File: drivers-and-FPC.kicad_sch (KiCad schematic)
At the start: 0 parts

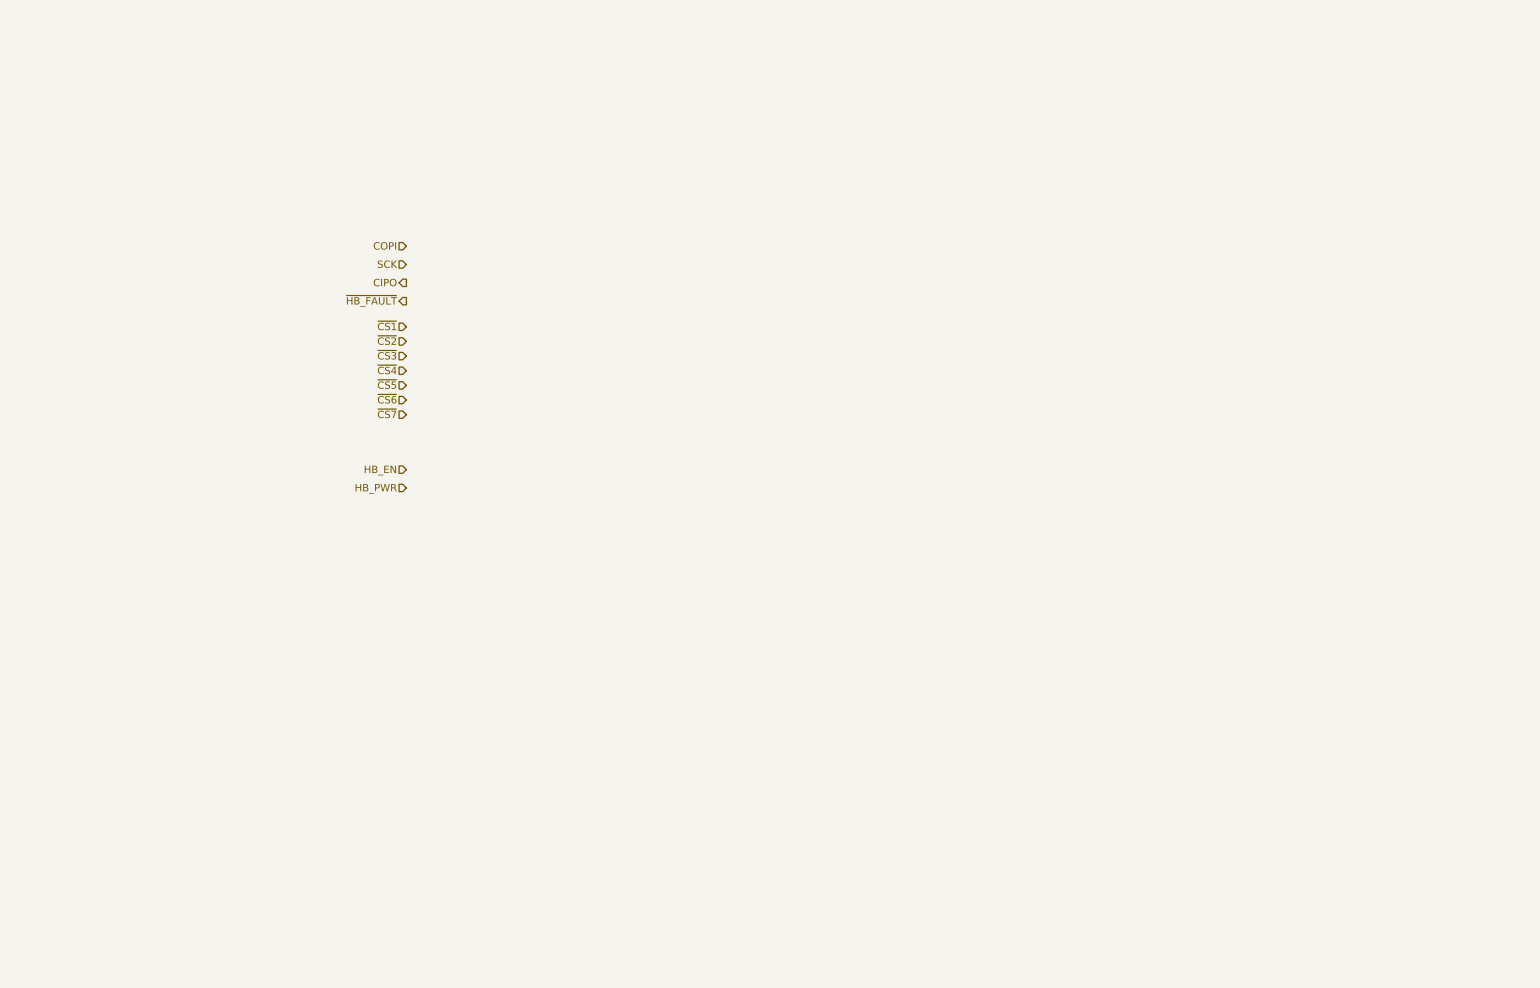
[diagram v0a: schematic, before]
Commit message: schematic rough draft except fpc
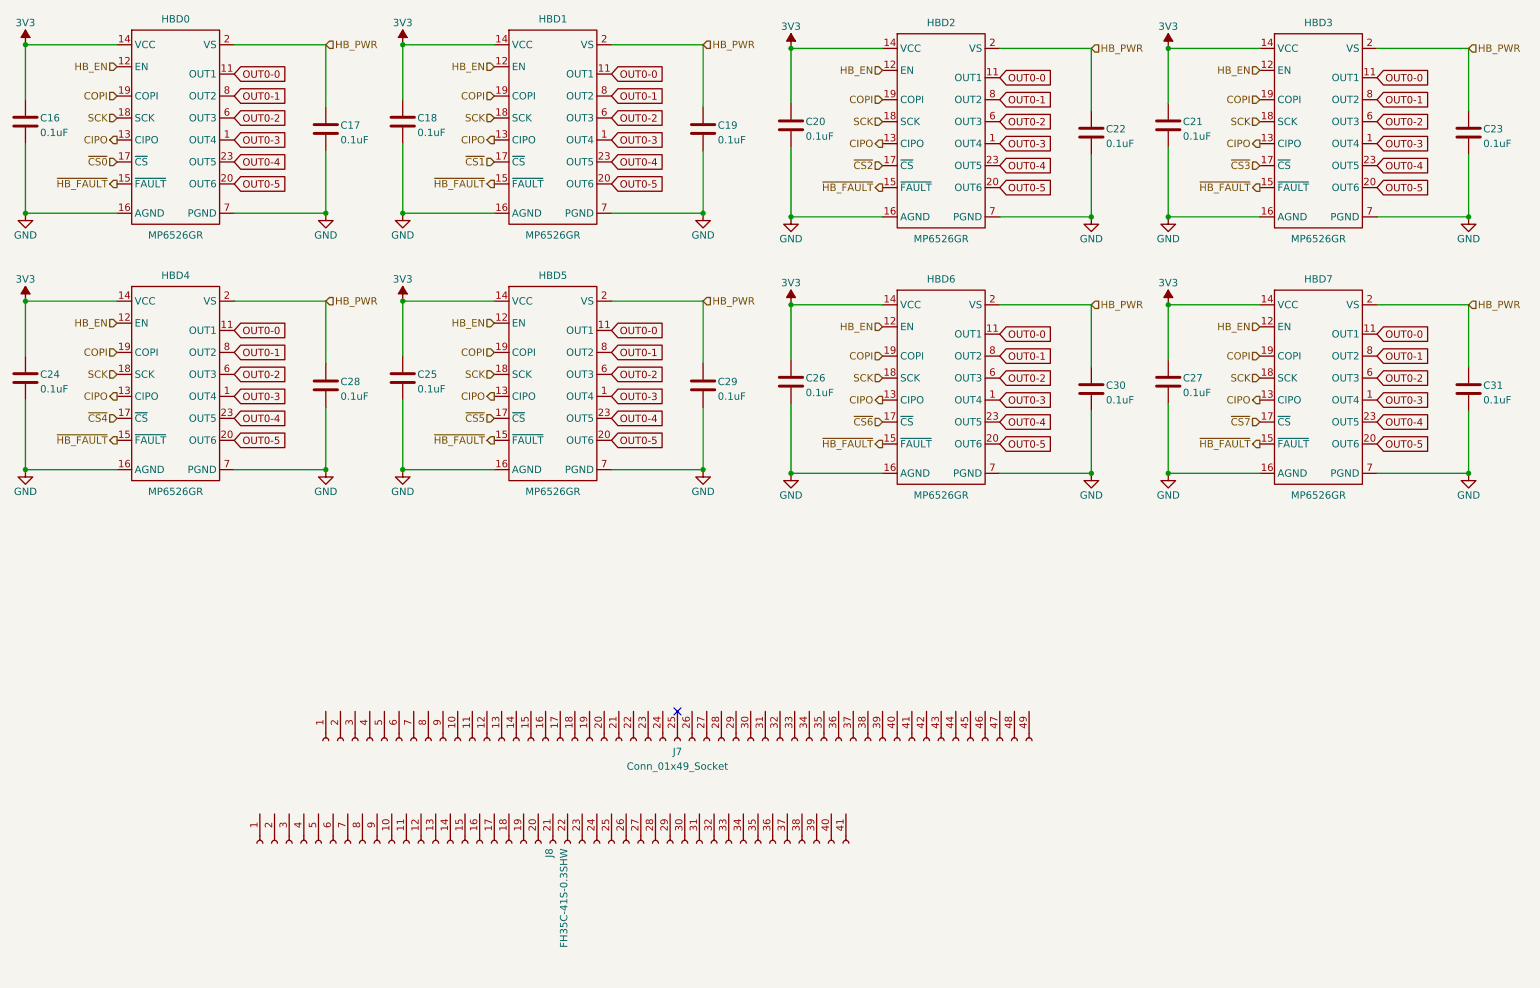
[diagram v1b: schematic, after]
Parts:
- added C16, C17, C18, C19, C20, C21, C22, C23, C24, C25, C26, C27, C28, C29, C30, C31: 0.1uF, Capacitor_SMD:C_0402_1005Metric, symbol Device:C
- added HBD0, HBD1, HBD2, HBD3, HBD4, HBD5, HBD6, HBD7: MP6526GR, Package_DFN_QFN:QFN-24-1EP_4x4mm_P0.5mm_EP2.7x2.7mm, symbol nrf52-controller:MP6526
- added J7: Conn_01x49_Socket, symbol Connector:Conn_01x49_Socket
- added J8: FH35C-41S-0.3SHW, v12e:CONN_FH35W-41S-0.3SHW, symbol v12e:Conn_01x41_Socket
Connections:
- net CIPO: now also HBD0.13 (CIPO), HBD1.13 (CIPO), HBD2.13 (CIPO), HBD3.13 (CIPO), HBD4.13 (CIPO), HBD5.13 (CIPO), HBD6.13 (CIPO), HBD7.13 (CIPO)
- net COPI: now also HBD0.19 (COPI), HBD1.19 (COPI), HBD2.19 (COPI), HBD3.19 (COPI), HBD4.19 (COPI), HBD5.19 (COPI), HBD6.19 (COPI), HBD7.19 (COPI)
- net HB_EN: now also HBD0.12 (EN), HBD1.12 (EN), HBD2.12 (EN), HBD3.12 (EN), HBD4.12 (EN), HBD5.12 (EN), HBD6.12 (EN), HBD7.12 (EN)
- net SCK: now also HBD0.18 (SCK), HBD1.18 (SCK), HBD2.18 (SCK), HBD3.18 (SCK), HBD4.18 (SCK), HBD5.18 (SCK), HBD6.18 (SCK), HBD7.18 (SCK)
- net ~{CS1}: now also HBD1.17 (~{CS})
- net ~{CS2}: now also HBD2.17 (~{CS})
- net ~{CS3}: now also HBD3.17 (~{CS})
- net ~{CS4}: now also HBD4.17 (~{CS})
- net ~{CS5}: now also HBD5.17 (~{CS})
- net ~{CS6}: now also HBD6.17 (~{CS})
- net ~{CS7}: now also HBD7.17 (~{CS})
- net ~{HB_FAULT}: now also HBD0.15 (~{FAULT}), HBD1.15 (~{FAULT}), HBD2.15 (~{FAULT}), HBD3.15 (~{FAULT}), HBD4.15 (~{FAULT}), HBD5.15 (~{FAULT}), HBD6.15 (~{FAULT}), HBD7.15 (~{FAULT})
- new net 3V3: C16.1, C18.1, C20.1, C21.1, C24.1, C25.1, C26.1, C27.1, HBD0.14 (VCC), HBD1.14 (VCC), HBD2.14 (VCC), HBD3.14 (VCC), HBD4.14 (VCC), HBD5.14 (VCC), HBD6.14 (VCC), HBD7.14 (VCC)
- new net GND: C16.2, C17.2, C18.2, C19.2, C20.2, C21.2, C22.2, C23.2, C24.2, C25.2, C26.2, C27.2, C28.2, C29.2, C30.2, C31.2, HBD0.10 (PGND), HBD0.16 (AGND), HBD0.21 (PGND), HBD0.22 (PGND), HBD0.24 (PGND), HBD0.7 (PGND), HBD0.9 (PGND), HBD1.10 (PGND), HBD1.16 (AGND), HBD1.21 (PGND), HBD1.22 (PGND), HBD1.24 (PGND), HBD1.7 (PGND), HBD1.9 (PGND), HBD2.10 (PGND), HBD2.16 (AGND), HBD2.21 (PGND), HBD2.22 (PGND), HBD2.24 (PGND), HBD2.7 (PGND), HBD2.9 (PGND), HBD3.10 (PGND), HBD3.16 (AGND), HBD3.21 (PGND), HBD3.22 (PGND), HBD3.24 (PGND), HBD3.7 (PGND), HBD3.9 (PGND), HBD4.10 (PGND), HBD4.16 (AGND), HBD4.21 (PGND), HBD4.22 (PGND), HBD4.24 (PGND), HBD4.7 (PGND), HBD4.9 (PGND), HBD5.10 (PGND), HBD5.16 (AGND), HBD5.21 (PGND), HBD5.22 (PGND), HBD5.24 (PGND), HBD5.7 (PGND), HBD5.9 (PGND), HBD6.10 (PGND), HBD6.16 (AGND), HBD6.21 (PGND), HBD6.22 (PGND), HBD6.24 (PGND), HBD6.7 (PGND), HBD6.9 (PGND), HBD7.10 (PGND), HBD7.16 (AGND), HBD7.21 (PGND), HBD7.22 (PGND), HBD7.24 (PGND), HBD7.7 (PGND), HBD7.9 (PGND)
- new net OUT0-0: HBD0.11 (OUT1), HBD1.11 (OUT1), HBD2.11 (OUT1), HBD3.11 (OUT1), HBD4.11 (OUT1), HBD5.11 (OUT1), HBD6.11 (OUT1), HBD7.11 (OUT1)
- new net OUT0-1: HBD0.8 (OUT2), HBD1.8 (OUT2), HBD2.8 (OUT2), HBD3.8 (OUT2), HBD4.8 (OUT2), HBD5.8 (OUT2), HBD6.8 (OUT2), HBD7.8 (OUT2)
- new net OUT0-2: HBD0.6 (OUT3), HBD1.6 (OUT3), HBD2.6 (OUT3), HBD3.6 (OUT3), HBD4.6 (OUT3), HBD5.6 (OUT3), HBD6.6 (OUT3), HBD7.6 (OUT3)
- new net OUT0-3: HBD0.1 (OUT4), HBD1.1 (OUT4), HBD2.1 (OUT4), HBD3.1 (OUT4), HBD4.1 (OUT4), HBD5.1 (OUT4), HBD6.1 (OUT4), HBD7.1 (OUT4)
- new net OUT0-4: HBD0.23 (OUT5), HBD1.23 (OUT5), HBD2.23 (OUT5), HBD3.23 (OUT5), HBD4.23 (OUT5), HBD5.23 (OUT5), HBD6.23 (OUT5), HBD7.23 (OUT5)
- new net OUT0-5: HBD0.20 (OUT6), HBD1.20 (OUT6), HBD2.20 (OUT6), HBD3.20 (OUT6), HBD4.20 (OUT6), HBD5.20 (OUT6), HBD6.20 (OUT6), HBD7.20 (OUT6)
- new net VS: C17.1, C19.1, C22.1, C23.1, C28.1, C29.1, C30.1, C31.1, HBD0.2 (VS), HBD0.3 (VS), HBD0.4 (VS), HBD0.5 (VS), HBD1.2 (VS), HBD1.3 (VS), HBD1.4 (VS), HBD1.5 (VS), HBD2.2 (VS), HBD2.3 (VS), HBD2.4 (VS), HBD2.5 (VS), HBD3.2 (VS), HBD3.3 (VS), HBD3.4 (VS), HBD3.5 (VS), HBD4.2 (VS), HBD4.3 (VS), HBD4.4 (VS), HBD4.5 (VS), HBD5.2 (VS), HBD5.3 (VS), HBD5.4 (VS), HBD5.5 (VS), HBD6.2 (VS), HBD6.3 (VS), HBD6.4 (VS), HBD6.5 (VS), HBD7.2 (VS), HBD7.3 (VS), HBD7.4 (VS), HBD7.5 (VS)
- new net ~{CS0}: HBD0.17 (~{CS})
- no-connect marks 0 -> 1

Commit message: schematic draft 2; no FPC connections, no testpoints
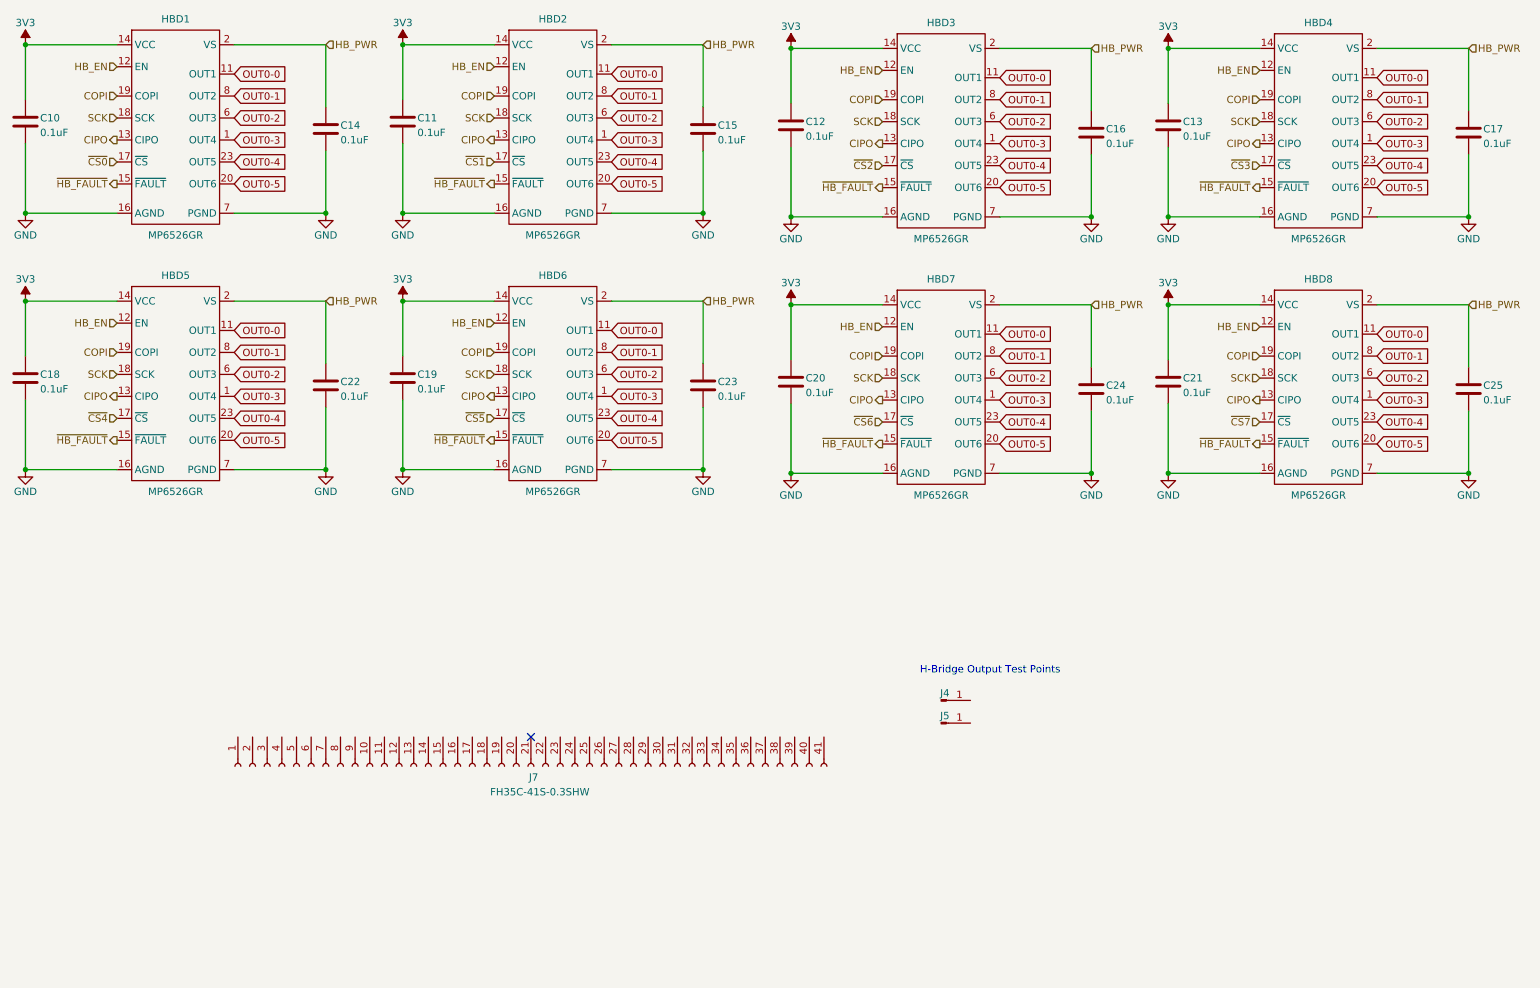
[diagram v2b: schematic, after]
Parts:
- removed J7: Conn_01x49_Socket, symbol Connector:Conn_01x49_Socket
- added J4, J5: Conn_01x01_Pin, nrf52-controller:TP_1mm, symbol Connector:Conn_01x01_Pin
- J7: renamed from J8; footprint v12e:CONN_FH35W-41S-0.3SHW -> nrf52-controller:CONN_FH35W-41S-0.3SHW
- renumbered C16 to C10, C18 to C11, C20 to C12, C21 to C13, C17 to C14, C19 to C15, C22 to C16, C23 to C17, C24 to C18, C25 to C19, C26 to C20, C27 to C21, C28 to C22, C29 to C23, C30 to C24, C31 to C25, HBD0 to HBD1, HBD1 to HBD2, HBD2 to HBD3, HBD3 to HBD4, HBD4 to HBD5, HBD5 to HBD6, HBD6 to HBD7, HBD7 to HBD8
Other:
- note added: "H-Bridge Output Test Points"
- moved on the sheet: J7

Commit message: layout start
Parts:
- removed C21, C25: 0.1uF, Capacitor_SMD:C_0402_1005Metric, symbol Device:C
- removed HBD8: MP6526GR, Package_DFN_QFN:QFN-24-1EP_4x4mm_P0.5mm_EP2.7x2.7mm, symbol nrf52-controller:MP6526
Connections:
- net GND: now also HBD1.25 (EPAD), HBD2.25 (EPAD), HBD3.25 (EPAD), HBD4.25 (EPAD), HBD5.25 (EPAD), HBD6.25 (EPAD), HBD7.25 (EPAD)
- net OUT0-0: no longer HBD2.11 (OUT1), HBD3.11 (OUT1), HBD4.11 (OUT1), HBD5.11 (OUT1), HBD6.11 (OUT1), HBD7.11 (OUT1)
- net OUT0-1: no longer HBD2.8 (OUT2), HBD3.8 (OUT2), HBD4.8 (OUT2), HBD5.8 (OUT2), HBD6.8 (OUT2), HBD7.8 (OUT2)
- net OUT0-2: no longer HBD2.6 (OUT3), HBD3.6 (OUT3), HBD4.6 (OUT3), HBD5.6 (OUT3), HBD6.6 (OUT3), HBD7.6 (OUT3)
- net OUT0-3: no longer HBD2.1 (OUT4), HBD3.1 (OUT4), HBD4.1 (OUT4), HBD5.1 (OUT4), HBD6.1 (OUT4), HBD7.1 (OUT4)
- net OUT0-4: no longer HBD2.23 (OUT5), HBD3.23 (OUT5), HBD4.23 (OUT5), HBD5.23 (OUT5), HBD6.23 (OUT5), HBD7.23 (OUT5)
- net OUT0-5: no longer HBD2.20 (OUT6), HBD3.20 (OUT6), HBD4.20 (OUT6), HBD5.20 (OUT6), HBD6.20 (OUT6), HBD7.20 (OUT6)
- new net OUT1-0: HBD2.11 (OUT1)
- new net OUT1-1: HBD2.8 (OUT2)
- new net OUT1-2: HBD2.6 (OUT3)
- new net OUT1-3: HBD2.1 (OUT4)
- new net OUT1-4: HBD2.23 (OUT5)
- new net OUT1-5: HBD2.20 (OUT6)
- new net OUT2-0: HBD3.11 (OUT1)
- new net OUT2-1: HBD3.8 (OUT2)
- new net OUT2-2: HBD3.6 (OUT3)
- new net OUT2-3: HBD3.1 (OUT4)
- new net OUT2-4: HBD3.23 (OUT5)
- new net OUT2-5: HBD3.20 (OUT6)
- new net OUT3-0: HBD4.11 (OUT1)
- new net OUT3-1: HBD4.8 (OUT2)
- new net OUT3-2: HBD4.6 (OUT3)
- new net OUT3-3: HBD4.1 (OUT4)
- new net OUT3-4: HBD4.23 (OUT5)
- new net OUT3-5: HBD4.20 (OUT6)
- new net OUT4-0: HBD5.11 (OUT1)
- new net OUT4-1: HBD5.8 (OUT2)
- new net OUT4-2: HBD5.6 (OUT3)
- new net OUT4-3: HBD5.1 (OUT4)
- new net OUT4-4: HBD5.23 (OUT5)
- new net OUT4-5: HBD5.20 (OUT6)
- new net OUT5-0: HBD6.11 (OUT1)
- new net OUT5-1: HBD6.8 (OUT2)
- new net OUT5-2: HBD6.6 (OUT3)
- new net OUT5-3: HBD6.1 (OUT4)
- new net OUT5-4: HBD6.23 (OUT5)
- new net OUT5-5: HBD6.20 (OUT6)
- new net OUT6-0: HBD7.11 (OUT1)
- new net OUT6-1: HBD7.8 (OUT2)
- new net OUT6-2: HBD7.6 (OUT3)
- new net OUT6-3: HBD7.1 (OUT4)
- new net OUT6-4: HBD7.23 (OUT5)
- new net OUT6-5: HBD7.20 (OUT6)
